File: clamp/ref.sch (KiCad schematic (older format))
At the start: 21 parts, among them P4 CONN_01X06, Q1 2N3904, U12 LTZ1000, U13 LM741, U14 LM741

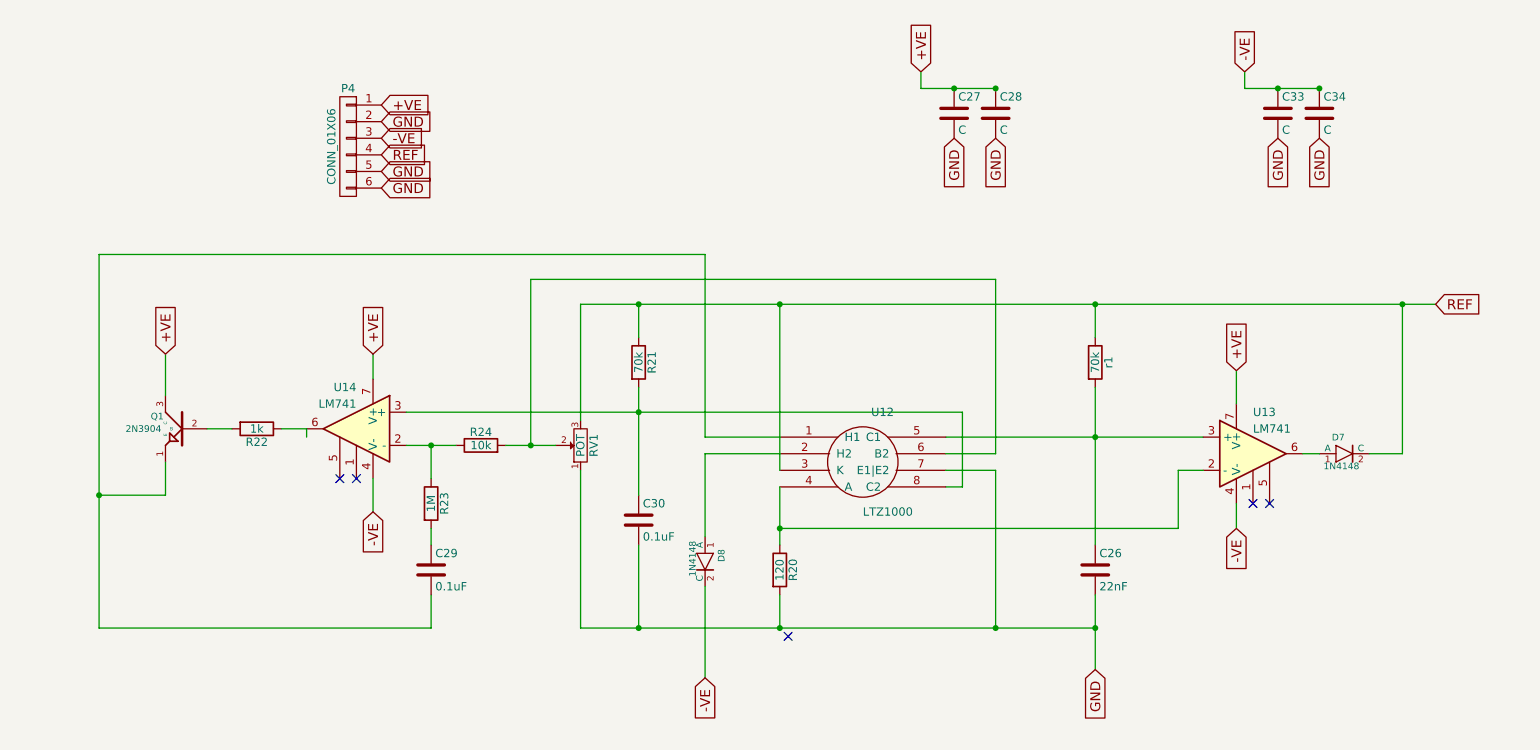
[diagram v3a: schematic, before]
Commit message: add resistor divider in place of pot
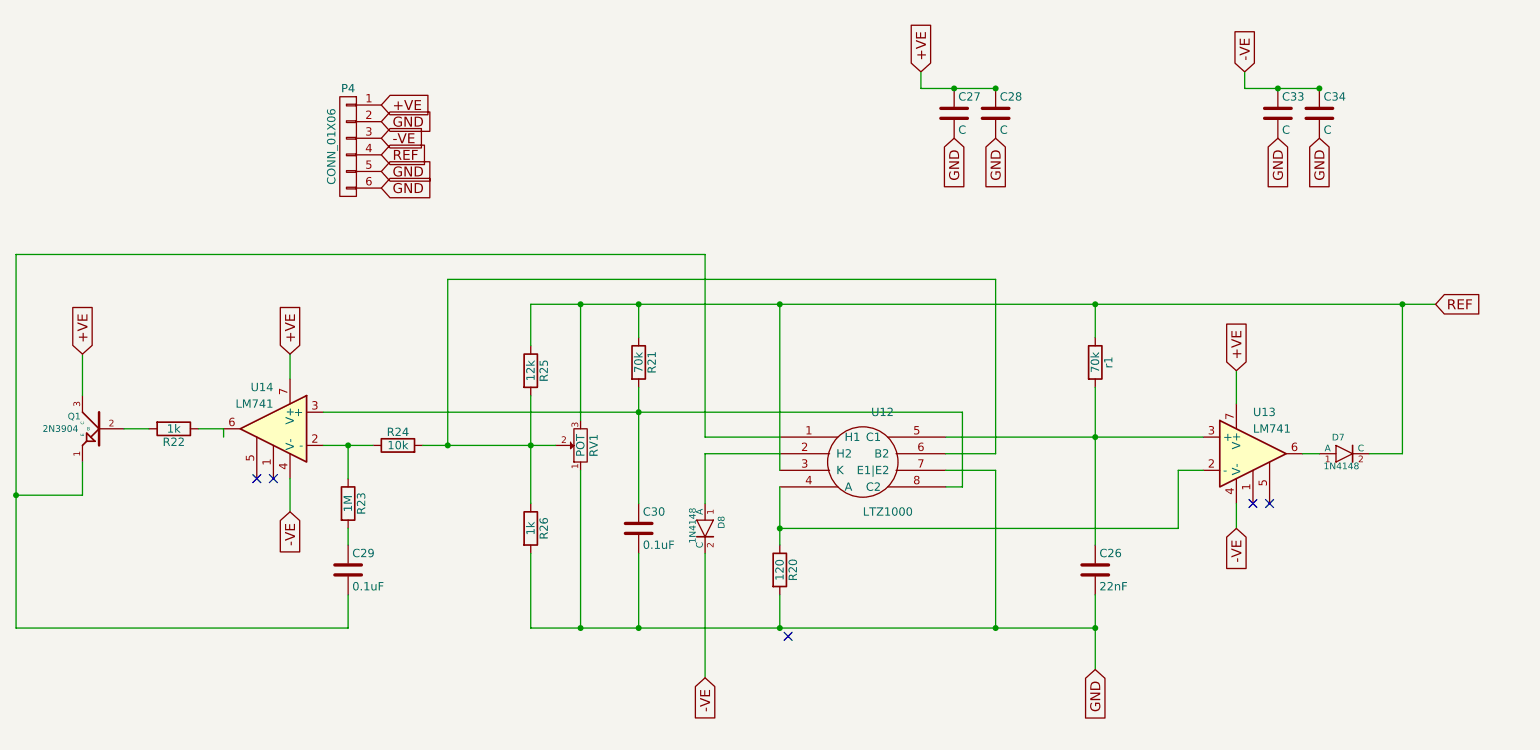
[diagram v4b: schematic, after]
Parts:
- added R25: 12k, Resistors_ThroughHole:Resistor_TO-220_Vertical, symbol R
- added R26: 1k, Resistors_ThroughHole:Resistor_TO-220_Vertical, symbol R
- R21: footprint (none) -> Resistors_ThroughHole:Resistor_TO-220_Vertical
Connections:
- net GND: now also R26.2
- net REF: now also R25.1
- net at R24.2, RV1.2, U12.6 (B2): now also R25.2, R26.1
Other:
- moved on the sheet: C29, C30, D8, Q1, R22, R23, R24, U14
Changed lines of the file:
@@
 Connection ~ 4650 2250
 Wire Wire Line
-	4650 2750 4650 3400
+	4650 2750 4650 3450
 $Comp
 L C C30
 U 1 1 58649B1A
-P 4650 3550
-F 0 "C30" H 4675 3650 50  0000 L CNN
-F 1 "0.1uF" H 4675 3450 50  0000 L CNN
-F 2 "Capacitors_SMD:C_1206" H 4688 3400 50  0001 C CNN
-F 3 "" H 4650 3550 50  0000 C CNN
-	1    4650 3550
-	1    0    0    -1
-$EndComp
-Wire Wire Line
-	4650 4200 4650 3700
+P 4650 3600
+F 0 "C30" H 4675 3700 50  0000 L CNN
+F 1 "0.1uF" H 4675 3500 50  0000 L CNN
+F 2 "Capacitors_SMD:C_1206" H 4688 3450 50  0001 C CNN
+F 3 "" H 4650 3600 50  0000 C CNN
+	1    4650 3600
+	1    0    0    -1
+$EndComp
+Wire Wire Line
+	4650 4200 4650 3750
 Connection ~ 4650 4200
 Connection ~ 4650 2900
@@
 L LM741 U14
 U 1 1 5864A0CC
-P 2950 3000
-F 0 "U14" H 2950 3250 50  0000 L CNN
-F 1 "LM741" H 2950 3150 50  0000 L CNN
-F 2 "SMD_Packages:SOIC-8-N" H 3000 3050 50  0001 C CNN
-F 3 "" H 3100 3150 50  0000 C CNN
-	1    2950 3000
+P 2450 3000
+F 0 "U14" H 2450 3250 50  0000 L CNN
+F 1 "LM741" H 2450 3150 50  0000 L CNN
+F 2 "SMD_Packages:SOIC-8-N" H 2500 3050 50  0001 C CNN
+F 3 "" H 2600 3150 50  0000 C CNN
+	1    2450 3000
 	-1   0    0    -1
 $EndComp
@@
 Connection ~ 5500 2250
 Wire Wire Line
-	3250 2900 6600 2900
+	2750 2900 6600 2900
 Wire Wire Line
 	4300 2250 4300 2950
@@
 L R R24
 U 1 1 5864B194
-P 3700 3100
-F 0 "R24" V 3780 3100 50  0000 C CNN
-F 1 "10k" V 3700 3100 50  0000 C CNN
-F 2 "Resistors_SMD:R_1206" V 3630 3100 50  0001 C CNN
-F 3 "" H 3700 3100 50  0000 C CNN
-	1    3700 3100
+P 3200 3100
+F 0 "R24" V 3280 3100 50  0000 C CNN
+F 1 "10k" V 3200 3100 50  0000 C CNN
+F 2 "Resistors_SMD:R_1206" V 3130 3100 50  0001 C CNN
+F 3 "" H 3200 3100 50  0000 C CNN
+	1    3200 3100
 	0    -1   -1   0
 $EndComp
 Wire Wire Line
-	3250 3100 3550 3100
-Wire Wire Line
-	3850 3100 4150 3100
+	2750 3100 3050 3100
+Wire Wire Line
+	3350 3100 4150 3100
 Text GLabel 5050 4500 3    60   Input ~ 0
 -VE
@@
 L R R23
 U 1 1 5864BDBF
-P 3400 3450
-F 0 "R23" V 3480 3450 50  0000 C CNN
-F 1 "1M" V 3400 3450 50  0000 C CNN
-F 2 "Resistors_SMD:R_1206" V 3330 3450 50  0001 C CNN
-F 3 "" H 3400 3450 50  0000 C CNN
-	1    3400 3450
+P 2900 3450
+F 0 "R23" V 2980 3450 50  0000 C CNN
+F 1 "1M" V 2900 3450 50  0000 C CNN
+F 2 "Resistors_SMD:R_1206" V 2830 3450 50  0001 C CNN
+F 3 "" H 2900 3450 50  0000 C CNN
+	1    2900 3450
 	1    0    0    -1
 $EndComp
@@
 L C C29
 U 1 1 5864BE17
-P 3400 3850
-F 0 "C29" H 3425 3950 50  0000 L CNN
-F 1 "0.1uF" H 3425 3750 50  0000 L CNN
-F 2 "Capacitors_SMD:C_1206" H 3438 3700 50  0001 C CNN
-F 3 "" H 3400 3850 50  0000 C CNN
-	1    3400 3850
-	1    0    0    -1
-$EndComp
-Wire Wire Line
-	3400 3600 3400 3700
-Wire Wire Line
-	3400 4000 3400 4200
-Wire Wire Line
-	3400 3100 3400 3300
-Connection ~ 3400 3100
+P 2900 3850
+F 0 "C29" H 2925 3950 50  0000 L CNN
+F 1 "0.1uF" H 2925 3750 50  0000 L CNN
+F 2 "Capacitors_SMD:C_1206" H 2938 3700 50  0001 C CNN
+F 3 "" H 2900 3850 50  0000 C CNN
+	1    2900 3850
+	1    0    0    -1
+$EndComp
+Wire Wire Line
+	2900 3600 2900 3700
+Wire Wire Line
+	2900 4000 2900 4200
+Wire Wire Line
+	2900 3100 2900 3300
+Connection ~ 2900 3100
 $Comp
 L 2N3904 Q1
 U 1 1 5864C22A
-P 1900 3000
-F 0 "Q1" H 2050 3075 40  0000 C CNN
-F 1 "2N3904" H 2025 3000 40  0000 L CNN
-F 2 "TO_SOT_Packages_SMD:SOT-23" H 1900 3000 60  0001 C CNN
-F 3 "" H 1900 3000 60  0001 C CNN
-	1    1900 3000
+P 1400 3000
+F 0 "Q1" H 1550 3075 40  0000 C CNN
+F 1 "2N3904" H 1525 3000 40  0000 L CNN
+F 2 "TO_SOT_Packages_SMD:SOT-23" H 1400 3000 60  0001 C CNN
+F 3 "" H 1400 3000 60  0001 C CNN
+	1    1400 3000
 	-1   0    0    -1
 $EndComp
-Text GLabel 1800 2550 1    60   Input ~ 0
+Text GLabel 1300 2550 1    60   Input ~ 0
 +VE
 Wire Wire Line
-	1800 2550 1800 2800
+	1300 2550 1300 2800
 $Comp
 L R R22
 U 1 1 5864C439
-P 2350 3000
-F 0 "R22" V 2430 3000 50  0000 C CNN
-F 1 "1k" V 2350 3000 50  0000 C CNN
-F 2 "Resistors_SMD:R_1206" V 2280 3000 50  0001 C CNN
-F 3 "" H 2350 3000 50  0000 C CNN
-	1    2350 3000
+P 1850 3000
+F 0 "R22" V 1930 3000 50  0000 C CNN
+F 1 "1k" V 1850 3000 50  0000 C CNN
+F 2 "Resistors_SMD:R_1206" V 1780 3000 50  0001 C CNN
+F 3 "" H 1850 3000 50  0000 C CNN
+	1    1850 3000
 	0    1    1    0
 $EndComp
 Wire Wire Line
-	2050 3000 2200 3000
-Wire Wire Line
-	2500 3000 2650 3000
-Wire Wire Line
-	2650 3000 2650 3050
-Wire Wire Line
-	1800 3400 1800 3200
-Wire Wire Line
-	1400 3400 1800 3400
-Wire Wire Line
-	1400 1950 1400 4200
-Wire Wire Line
-	1400 1950 5050 1950
+	1550 3000 1700 3000
+Wire Wire Line
+	2000 3000 2150 3000
+Wire Wire Line
+	2150 3000 2150 3050
+Wire Wire Line
+	1300 3400 1300 3200
+Wire Wire Line
+	900  3400 1300 3400
+Wire Wire Line
+	900  1950 900  4200
+Wire Wire Line
+	900  1950 5050 1950
 Wire Wire Line
 	5050 1950 5050 3050
 Wire Wire Line
-	4300 2250 9450 2250
-Wire Wire Line
-	4300 4200 7400 4200
+	4000 2250 9450 2250
+Wire Wire Line
+	4000 4200 7400 4200
 Wire Wire Line
 	5500 3600 7900 3600
 Wire Wire Line
 	8650 3150 8750 3150
-Text GLabel 3050 2550 1    60   Input ~ 0
+Text GLabel 2550 2550 1    60   Input ~ 0
 +VE
-Text GLabel 3050 3500 3    60   Input ~ 0
+Text GLabel 2550 3500 3    60   Input ~ 0
 -VE
 Wire Wire Line
-	3050 3500 3050 3300
-Wire Wire Line
-	3050 2550 3050 2700
-NoConn ~ 2850 3300
-NoConn ~ 2950 3300
+	2550 3500 2550 3300
+Wire Wire Line
+	2550 2550 2550 2700
+NoConn ~ 2350 3300
+NoConn ~ 2450 3300
 Wire Wire Line
 	6500 3050 8050 3050
@@
 	6800 2100 6800 3150
 Wire Wire Line
-	4000 2100 4000 3100
-Connection ~ 4000 3100
-Wire Wire Line
-	6800 2100 4000 2100
-Wire Wire Line
-	1400 4200 3400 4200
-Connection ~ 1400 3400
+	3500 2100 3500 3100
+Connection ~ 3500 3100
+Wire Wire Line
+	6800 2100 3500 2100
+Wire Wire Line
+	900  4200 2900 4200
+Connection ~ 900  3400
 $Comp
 L 1N4148 D8
 U 1 1 5864EF9B
-P 5050 3800
-F 0 "D8" H 4975 3875 40  0000 L BNN
-F 1 "1N4148" H 4925 3725 40  0000 L CNN
-F 2 "Diodes_SMD:MiniMELF_Standard" H 5050 3950 30  0001 C CNN
-F 3 "" H 5050 3800 60  0000 C CNN
-	1    5050 3800
+P 5050 3600
+F 0 "D8" H 4975 3675 40  0000 L BNN
+F 1 "1N4148" H 4925 3525 40  0000 L CNN
+F 2 "Diodes_SMD:MiniMELF_Standard" H 5050 3750 30  0001 C CNN
+F 3 "" H 5050 3600 60  0000 C CNN
+	1    5050 3600
 	0    1    1    0
 $EndComp
 Wire Wire Line
-	5050 3150 5050 3650
-Wire Wire Line
-	5050 3950 5050 4500
+	5050 3150 5050 3450
+Wire Wire Line
+	5050 3750 5050 4500
 Wire Wire Line
 	5050 3050 5500 3050
@@
 F 0 "R21" V 4730 2600 50  0000 C CNN
 F 1 "70k" V 4650 2600 50  0000 C CNN
-F 2 "" V 4580 2600 50  0001 C CNN
+F 2 "Resistors_ThroughHole:Resistor_TO-220_Vertical" V 4580 2600 50  0001 C CNN
 F 3 "" H 4650 2600 50  0000 C CNN
 	1    4650 2600
 	1    0    0    -1
 $EndComp
+$Comp
+L R R25
+U 1 1 5865B477
+P 4000 2650
+F 0 "R25" V 4080 2650 50  0000 C CNN
+F 1 "12k" V 4000 2650 50  0000 C CNN
+F 2 "Resistors_ThroughHole:Resistor_TO-220_Vertical" V 3930 2650 50  0001 C CNN
+F 3 "" H 4000 2650 50  0000 C CNN
+	1    4000 2650
+	1    0    0    -1
+$EndComp
+$Comp
+L R R26
+U 1 1 5865B4EC
+P 4000 3600
+F 0 "R26" V 4080 3600 50  0000 C CNN
+F 1 "1k" V 4000 3600 50  0000 C CNN
+F 2 "Resistors_ThroughHole:Resistor_TO-220_Vertical" V 3930 3600 50  0001 C CNN
+F 3 "" H 4000 3600 50  0000 C CNN
+	1    4000 3600
+	1    0    0    -1
+$EndComp
+Wire Wire Line
+	4000 2250 4000 2500
+Connection ~ 4300 2250
+Wire Wire Line
+	4000 2800 4000 3450
+Connection ~ 4000 3100
+Wire Wire Line
+	4000 3750 4000 4200
+Connection ~ 4300 4200
 $EndSCHEMATC
